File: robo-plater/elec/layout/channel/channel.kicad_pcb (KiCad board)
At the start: 2 copper layers, 20 parts, among them J1 ?, U1 ?, U2 ?, U3 ?, U4 ?, U5 ?

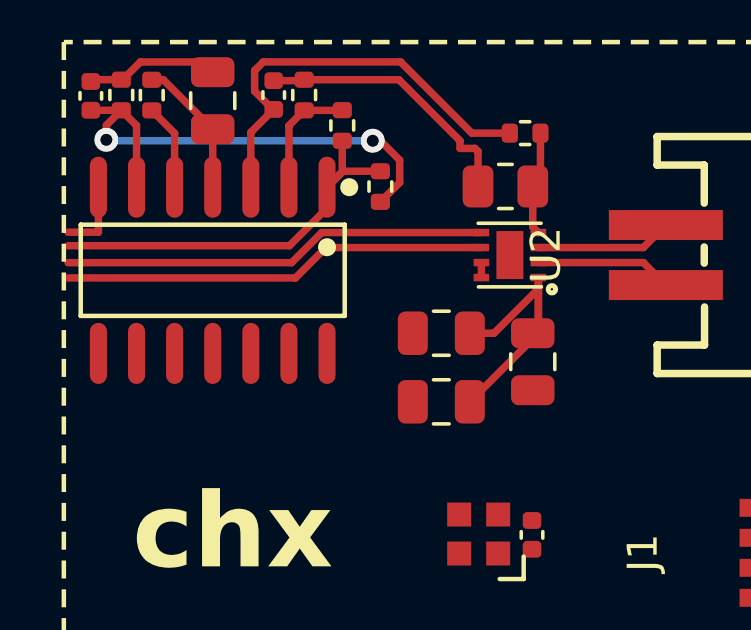
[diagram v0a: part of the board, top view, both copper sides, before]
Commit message: Add stemma/quuic connectors and load cell amps
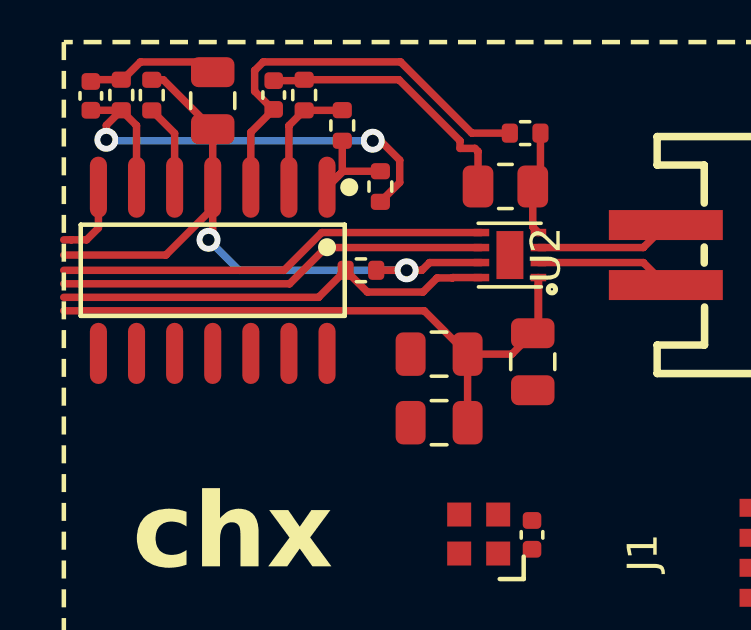
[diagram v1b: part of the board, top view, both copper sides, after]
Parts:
- added R1: 62.5mW Thick Film Resistors 50V ±100ppm/℃ ±1% 10kΩ 0402 Chi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, lib:R0402, F.Cu at (126.7, 64.8)
- moved C1 0.70 mm to (129.3, 69.8)
- moved C2 0.70 mm to (129.3, 67.6)
- renumbered R1 to R2, R2 to R3, R3 to R4, R4 to R5, R5 to R6, R6 to R7, R7 to R8
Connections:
- U1 pad 8: motor_driver-vcc-1 -> enable
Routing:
- net motor_driver-vcc-1: track 5.15 -> 23.4 mm, vias 0 -> 2
- net enable: track 0.00 -> 14.8 mm
- net motor_driver-vcc: track 10.0 -> 22.7 mm
- net current: track 13.6 -> 4.46 mm

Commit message: Layout v0.1 done
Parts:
- moved R3 89.9 mm to (51.7, 100.0), turned to -90 degrees
- moved R5 88.8 mm to (50.4, 107.4), turned to 180 degrees
- moved U2 88.7 mm to (55.7, 92.4), turned to 180 degrees
- moved C5 88.6 mm to (50.4, 108.4), turned to 180 degrees
- moved U3 88.2 mm to (52.2, 102.2), turned to 90 degrees
- moved R4 87.8 mm to (51.4, 106.1), turned to 180 degrees
- moved C4 87.8 mm to (50.6, 110.4), turned to 180 degrees
- moved R7 87.6 mm to (50.4, 112.5), turned to 180 degrees
- moved R8 87.5 mm to (50.4, 113.5), turned to 180 degrees
- moved C6 87.3 mm to (50.4, 114.5), turned to 180 degrees
- moved R2 87.2 mm to (53.5, 100.7), turned to -90 degrees
- moved R6 85.5 mm to (53.5, 104.9), turned to 0 degrees
- moved U1 84.2 mm to (55.7, 100.5), turned to -90 degrees
- moved R1 81.4 mm to (56.3, 105.5), turned to 90 degrees
- moved U4 79.9 mm to (56.3, 110.4), turned to -90 degrees
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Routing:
- net pwm: track 14.4 -> 0.00 mm
- net dir: track 14.4 -> 0.00 mm
- net in1_plus: track 14.1 -> 2.91 mm
- net _shunt_gnd: track 7.32 -> 1.03 mm
- net pulses: track 2.68 -> 0.00 mm
